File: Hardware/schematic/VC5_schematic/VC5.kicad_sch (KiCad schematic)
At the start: 2 parts, among them J1 Debug_output

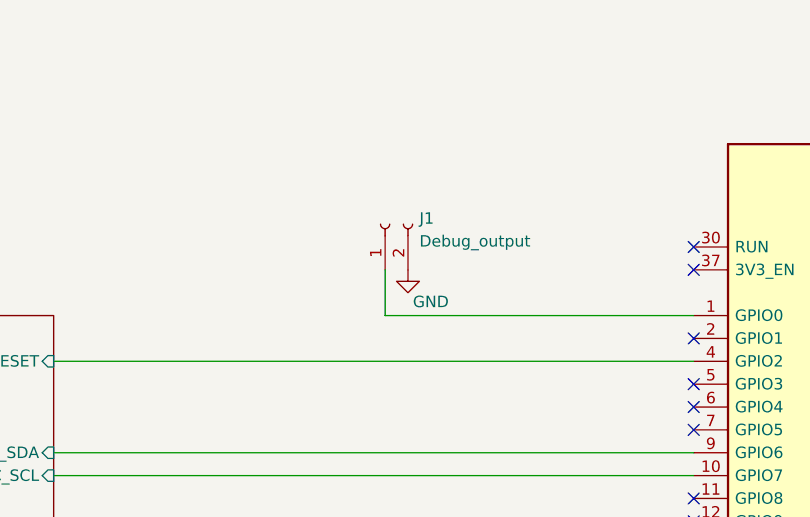
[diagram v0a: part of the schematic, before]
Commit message: fixed an error in the filters for the rotaries
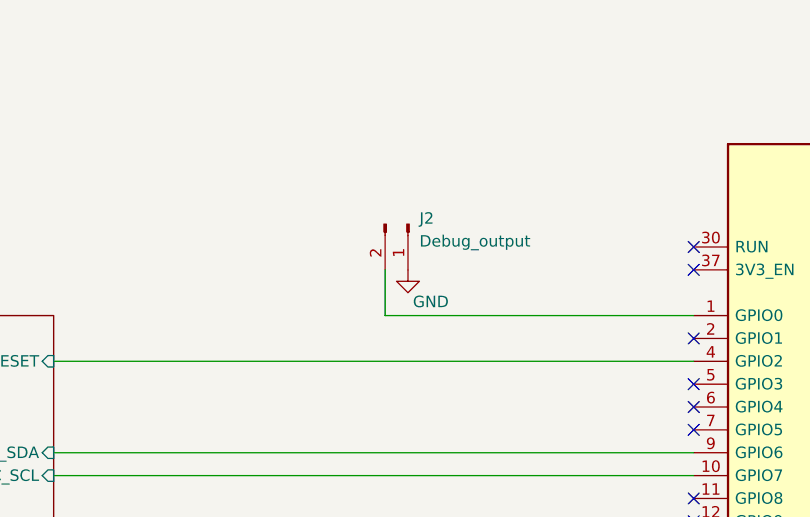
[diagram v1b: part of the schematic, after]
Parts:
- removed J1: Debug_output, symbol Connector:Conn_01x02_Socket
- added J2: Debug_output, Connector_PinHeader_2.54mm:PinHeader_1x02_P2.54mm_Vertical, symbol Connector:Conn_01x02_Pin
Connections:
- net GND: now also J2.1 (Pin_1)
- net at A1.1 (GPIO0): now also J2.2 (Pin_2)
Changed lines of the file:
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@@
-	)
-	(symbol
-		(lib_id "Connector:Conn_01x02_Socket")
-		(at 96.52 45.72 90)
-		(unit 1)
-		(exclude_from_sim no)
-		(in_bom yes)
-		(on_board yes)
-		(dnp no)
-		(fields_autoplaced yes)
-		(property "Reference" "J1"
-			(at 100.33 45.0849 90)
-			(effects
-				(font
-					(size 1.27 1.27)
-				)
-				(justify right)
-			)
-		)
-		(property "Value" "Debug_output"
-			(at 100.33 47.6249 90)
-			(effects
-				(font
-					(size 1.27 1.27)
-				)
-				(justify right)
-			)
-		)
-		(property "Footprint" ""
-			(at 96.52 45.72 0)
-			(effects
-				(font
-					(size 1.27 1.27)
-				)
-				(hide yes)
-			)
-		)
-		(property "Datasheet" "~"
-			(at 96.52 45.72 0)
-			(effects
-				(font
-					(size 1.27 1.27)
-				)
-				(hide yes)
-			)
-		)
-		(property "Description" "Generic connector, single row, 01x02, script generated"
-			(at 96.52 45.72 0)
-			(effects
-				(font
-					(size 1.27 1.27)
-				)
-				(hide yes)
-			)
-		)
-		(pin "1"
-		)
-		(pin "2"
-		)
-		(instances
-			(project ""
-				(path "/5ac87209-2525-401a-b136-a9d04031b521"
-					(reference "J1")
-					(unit 1)
-				)
-			)
-		)
 	)
 	(symbol
@@
 					(unit 1)
 				)
+			)
+		)
+	)
+	(symbol
+		(lib_id "Connector:Conn_01x02_Pin")
+		(at 99.06 45.72 270)
+		(unit 1)
+		(exclude_from_sim no)
+		(in_bom yes)
+		(on_board yes)
+		(dnp no)
+		(fields_autoplaced yes)
+		(property "Reference" "J2"
+			(at 100.33 45.0849 90)
+			(effects
+				(font
+					(size 1.27 1.27)
+				)
+				(justify left)
+			)
+		)
+		(property "Value" "Debug_output"
+			(at 100.33 47.6249 90)
+			(effects
+				(font
+					(size 1.27 1.27)
+				)
+				(justify left)
+			)
+		)
+		(property "Footprint" "Connector_PinHeader_2.54mm:PinHeader_1x02_P2.54mm_Vertical"
+			(at 99.06 45.72 0)
+			(effects
+				(font
+					(size 1.27 1.27)
+				)
+				(hide yes)
+			)
+		)
+		(property "Datasheet" "~"
+			(at 99.06 45.72 0)
+			(effects
+				(font
+					(size 1.27 1.27)
+				)
+				(hide yes)
+			)
+		)
+		(property "Description" "Generic connector, single row, 01x02, script generated"
+			(at 99.06 45.72 0)
+			(effects
+				(font
+					(size 1.27 1.27)
+				)
+				(hide yes)
+			)
+		)
+		(pin "1"
+		)
+		(pin "2"
+		)
+		(instances
+			(project ""
+				(path "/5ac87209-2525-401a-b136-a9d04031b521"
+					(reference "J2")
+					(unit 1)
+				)

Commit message: updated footprints and corresponding 3D models
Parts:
- A1: footprint Module:RaspberryPi_Pico_Common_THT -> VC5_footprint_library:RaspberryPi_Pico_Common_THT_custom
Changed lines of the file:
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@@
 			)
 		)
-		(property "Footprint" "Module:RaspberryPi_Pico_Common_THT"
+		(property "Footprint" "VC5_footprint_library:RaspberryPi_Pico_Common_THT_custom"
 			(at 153.67 118.11 0)
 			(effects

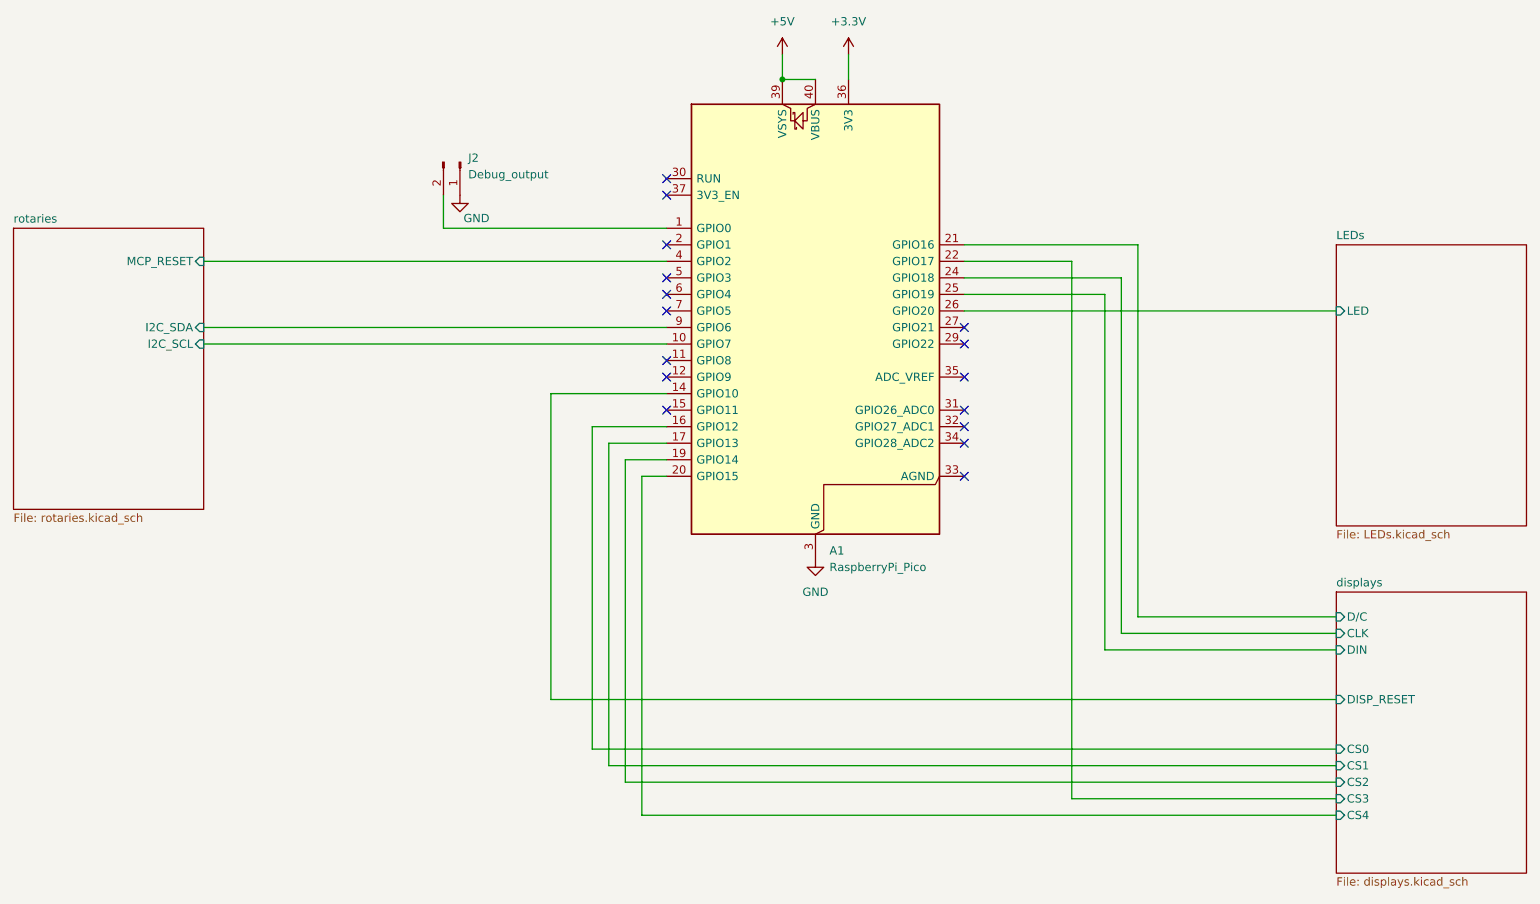
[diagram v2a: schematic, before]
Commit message: trace routing completed
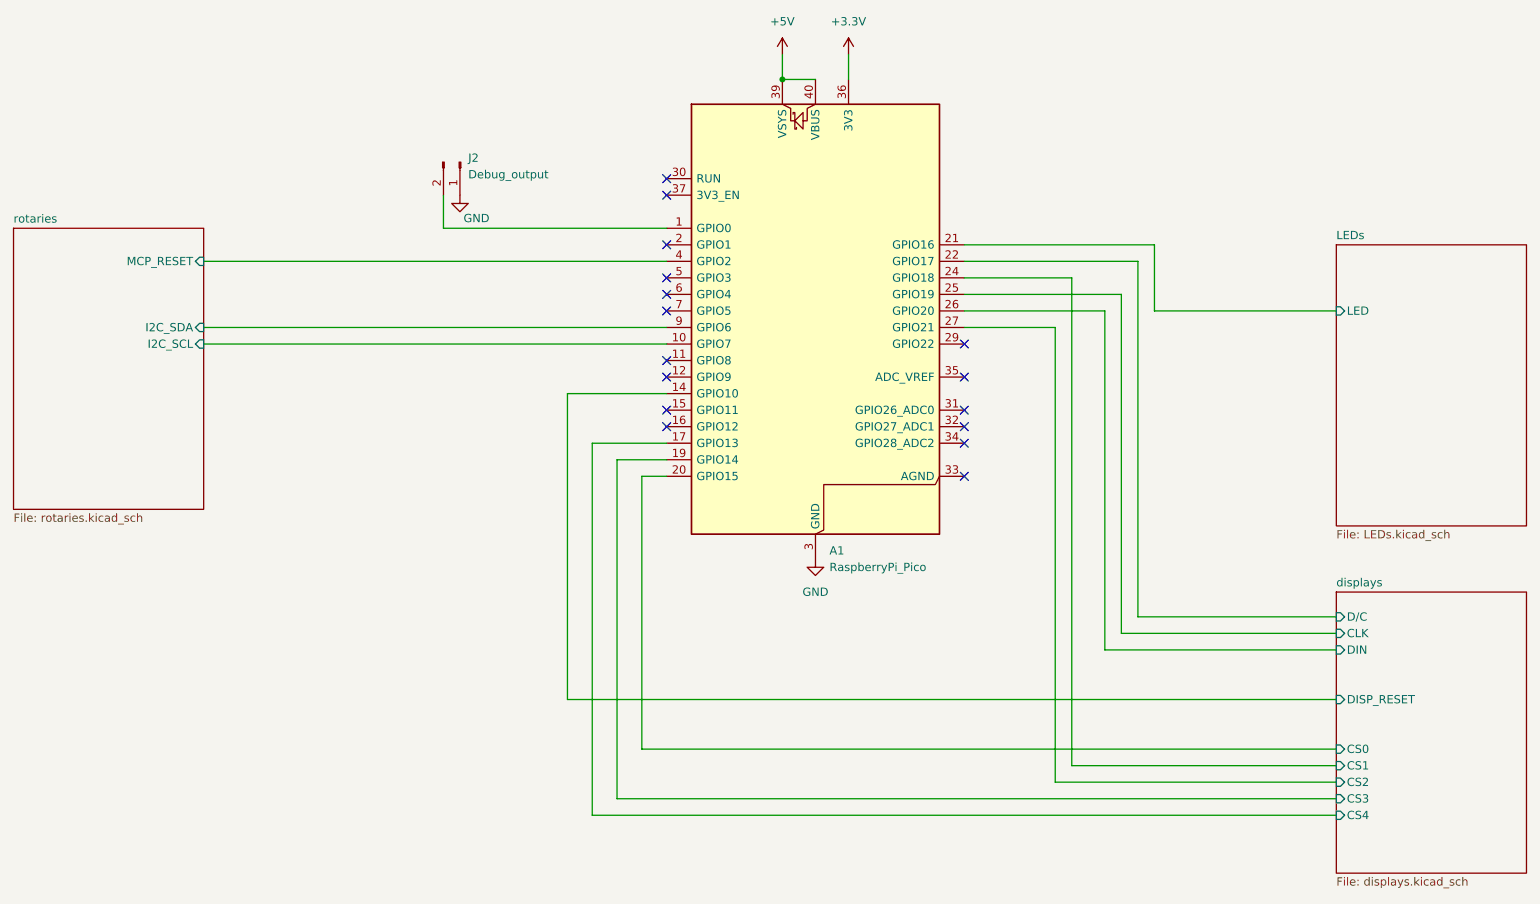
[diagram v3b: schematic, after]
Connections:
- net LEDs/LED: now also A1.21 (GPIO16); no longer A1.26 (GPIO20)
- net displays/CLK: now also A1.25 (GPIO19); no longer A1.24 (GPIO18)
- net displays/CS0: now also A1.20 (GPIO15); no longer A1.16 (GPIO12)
- net displays/CS1: now also A1.24 (GPIO18); no longer A1.17 (GPIO13)
- net displays/CS2: now also A1.27 (GPIO21); no longer A1.19 (GPIO14)
- net displays/CS3: now also A1.19 (GPIO14); no longer A1.22 (GPIO17)
- net displays/CS4: now also A1.17 (GPIO13); no longer A1.20 (GPIO15)
- net displays/DIN: now also A1.26 (GPIO20); no longer A1.25 (GPIO19)
- net displays/D/C: now also A1.22 (GPIO17); no longer A1.21 (GPIO16)
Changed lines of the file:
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@@
+	)
+	(no_connect
+		(at 130.81 86.36)
 	)
 	(no_connect
@@
 	)
 	(no_connect
-		(at 176.53 71.12)
-	)
-	(no_connect
 		(at 130.81 78.74)
 	)
@@
 	(wire
 		(pts
-			(xy 203.2 115.57) (xy 203.2 58.42)
-		)
-		(stroke
-			(width 0)
-			(type default)
-		)
-	)
-	(wire
-		(pts
-			(xy 124.46 91.44) (xy 130.81 91.44)
+			(xy 176.53 71.12) (xy 190.5 71.12)
+		)
+		(stroke
+			(width 0)
+			(type default)
+		)
+	)
+	(wire
+		(pts
+			(xy 203.2 115.57) (xy 203.2 60.96)
 		)
 		(stroke
@@
 	(wire
 		(pts
-			(xy 121.92 88.9) (xy 130.81 88.9)
+			(xy 190.5 140.97) (xy 233.68 140.97)
 		)
 		(stroke
@@
 	(wire
 		(pts
-			(xy 200.66 63.5) (xy 176.53 63.5)
-		)
-		(stroke
-			(width 0)
-			(type default)
-		)
-	)
-	(wire
-		(pts
-			(xy 113.03 128.27) (xy 113.03 81.28)
-		)
-		(stroke
-			(width 0)
-			(type default)
-		)
-	)
-	(wire
-		(pts
-			(xy 198.12 66.04) (xy 176.53 66.04)
-		)
-		(stroke
-			(width 0)
-			(type default)
-		)
-	)
-	(wire
-		(pts
-			(xy 121.92 138.43) (xy 121.92 88.9)
-		)
-		(stroke
-			(width 0)
-			(type default)
-		)
-	)
-	(wire
-		(pts
-			(xy 200.66 118.11) (xy 200.66 63.5)
+			(xy 193.04 138.43) (xy 233.68 138.43)
+		)
+		(stroke
+			(width 0)
+			(type default)
+		)
+	)
+	(wire
+		(pts
+			(xy 115.57 128.27) (xy 115.57 81.28)
+		)
+		(stroke
+			(width 0)
+			(type default)
+		)
+	)
+	(wire
+		(pts
+			(xy 119.38 146.05) (xy 233.68 146.05)
+		)
+		(stroke
+			(width 0)
+			(type default)
+		)
+	)
+	(wire
+		(pts
+			(xy 119.38 88.9) (xy 130.81 88.9)
+		)
+		(stroke
+			(width 0)
+			(type default)
+		)
+	)
+	(wire
+		(pts
+			(xy 127 93.98) (xy 127 135.89)
+		)
+		(stroke
+			(width 0)
+			(type default)
+		)
+	)
+	(wire
+		(pts
+			(xy 200.66 118.11) (xy 200.66 66.04)
 		)
 		(stroke
@@
 	(wire
 		(pts
-			(xy 198.12 120.65) (xy 198.12 66.04)
-		)
-		(stroke
-			(width 0)
-			(type default)
-		)
-	)
-	(wire
-		(pts
-			(xy 193.04 143.51) (xy 233.68 143.51)
-		)
-		(stroke
-			(width 0)
-			(type default)
-		)
-	)
-	(wire
-		(pts
-			(xy 119.38 86.36) (xy 130.81 86.36)
+			(xy 193.04 63.5) (xy 193.04 138.43)
+		)
+		(stroke
+			(width 0)
+			(type default)
+		)
+	)
+	(wire
+		(pts
+			(xy 198.12 120.65) (xy 198.12 68.58)
+		)
+		(stroke
+			(width 0)
+			(type default)
+		)
+	)
+	(wire
+		(pts
+			(xy 127 135.89) (xy 233.68 135.89)
+		)
+		(stroke
+			(width 0)
+			(type default)
+		)
+	)
+	(wire
+		(pts
+			(xy 123.19 91.44) (xy 130.81 91.44)
+		)
+		(stroke
+			(width 0)
+			(type default)
+		)
+	)
+	(wire
+		(pts
+			(xy 176.53 66.04) (xy 200.66 66.04)
 		)
 		(stroke
@@
 	(wire
 		(pts
-			(xy 124.46 140.97) (xy 124.46 91.44)
-		)
-		(stroke
-			(width 0)
-			(type default)
-		)
-	)
-	(wire
-		(pts
-			(xy 113.03 81.28) (xy 130.81 81.28)
-		)
-		(stroke
-			(width 0)
-			(type default)
-		)
-	)
-	(wire
-		(pts
-			(xy 124.46 140.97) (xy 233.68 140.97)
-		)
-		(stroke
-			(width 0)
-			(type default)
-		)
-	)
-	(wire
-		(pts
-			(xy 113.03 128.27) (xy 233.68 128.27)
-		)
-		(stroke
-			(width 0)
-			(type default)
-		)
-	)
-	(wire
-		(pts
-			(xy 127 146.05) (xy 233.68 146.05)
-		)
-		(stroke
-			(width 0)
-			(type default)
-		)
-	)
-	(wire
-		(pts
-			(xy 121.92 138.43) (xy 233.68 138.43)
+			(xy 115.57 81.28) (xy 130.81 81.28)
+		)
+		(stroke
+			(width 0)
+			(type default)
+		)
+	)
+	(wire
+		(pts
+			(xy 123.19 143.51) (xy 123.19 91.44)
+		)
+		(stroke
+			(width 0)
+			(type default)
+		)
+	)
+	(wire
+		(pts
+			(xy 123.19 143.51) (xy 233.68 143.51)
+		)
+		(stroke
+			(width 0)
+			(type default)
+		)
+	)
+	(wire
+		(pts
+			(xy 205.74 58.42) (xy 176.53 58.42)
+		)
+		(stroke
+			(width 0)
+			(type default)
+		)
+	)
+	(wire
+		(pts
+			(xy 119.38 146.05) (xy 119.38 88.9)
+		)
+		(stroke
+			(width 0)
+			(type default)
+		)
+	)
+	(wire
+		(pts
+			(xy 130.81 93.98) (xy 127 93.98)
+		)
+		(stroke
+			(width 0)
+			(type default)
+		)
+	)
+	(wire
+		(pts
+			(xy 115.57 128.27) (xy 233.68 128.27)
+		)
+		(stroke
+			(width 0)
+			(type default)
+		)
+	)
+	(wire
+		(pts
+			(xy 176.53 63.5) (xy 193.04 63.5)
 		)
 		(stroke
@@
 	(wire
 		(pts
-			(xy 119.38 135.89) (xy 119.38 86.36)
-		)
-		(stroke
-			(width 0)
-			(type default)
-		)
-	)
-	(wire
-		(pts
-			(xy 127 93.98) (xy 130.81 93.98)
-		)
-		(stroke
-			(width 0)
-			(type default)
-		)
-	)
-	(wire
-		(pts
-			(xy 193.04 143.51) (xy 193.04 60.96)
+			(xy 233.68 68.58) (xy 205.74 68.58)
 		)
 		(stroke
@@
 	(wire
 		(pts
-			(xy 119.38 135.89) (xy 233.68 135.89)
-		)
-		(stroke
-			(width 0)
-			(type default)
-		)
-	)
-	(wire
-		(pts
-			(xy 127 146.05) (xy 127 93.98)
-		)
-		(stroke
-			(width 0)
-			(type default)
-		)
-	)
-	(wire
-		(pts
-			(xy 176.53 68.58) (xy 233.68 68.58)
+			(xy 176.53 68.58) (xy 198.12 68.58)
+		)
+		(stroke
+			(width 0)
+			(type default)
+		)
+	)
+	(wire
+		(pts
+			(xy 205.74 68.58) (xy 205.74 58.42)
+		)
+		(stroke
+			(width 0)
+			(type default)
+		)
+	)
+	(wire
+		(pts
+			(xy 190.5 71.12) (xy 190.5 140.97)
 		)
 		(stroke
@@
 	(wire
 		(pts
-			(xy 193.04 60.96) (xy 176.53 60.96)
-		)
-		(stroke
-			(width 0)
-			(type default)
-		)
-	)
-	(wire
-		(pts
-			(xy 203.2 58.42) (xy 176.53 58.42)
-		)
-		(stroke
+			(xy 176.53 60.96) (xy 203.2 60.96)
+		)
+		(stroke

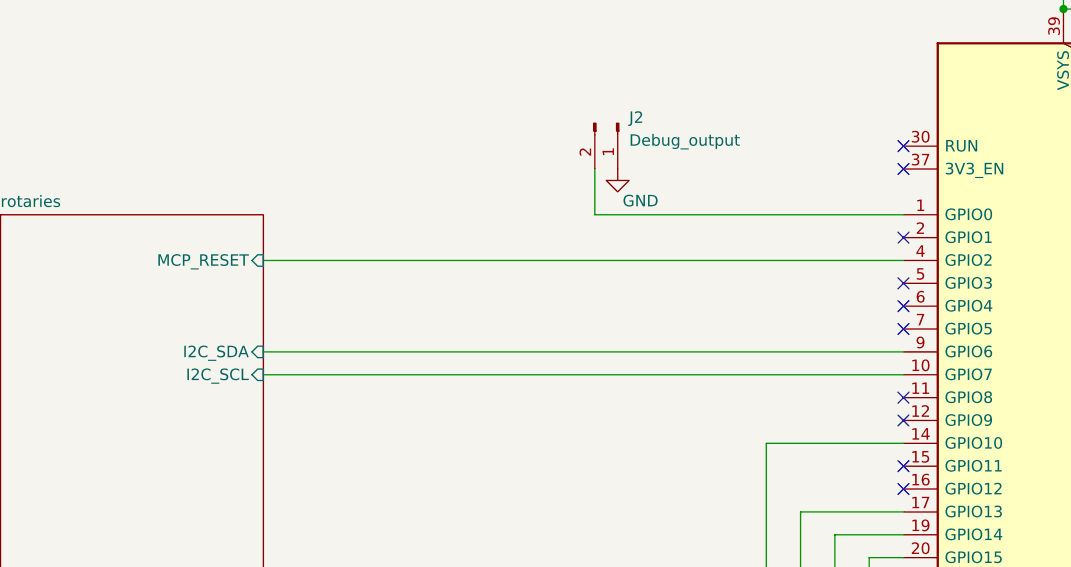
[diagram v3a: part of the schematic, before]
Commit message: fixed missing interrupt line
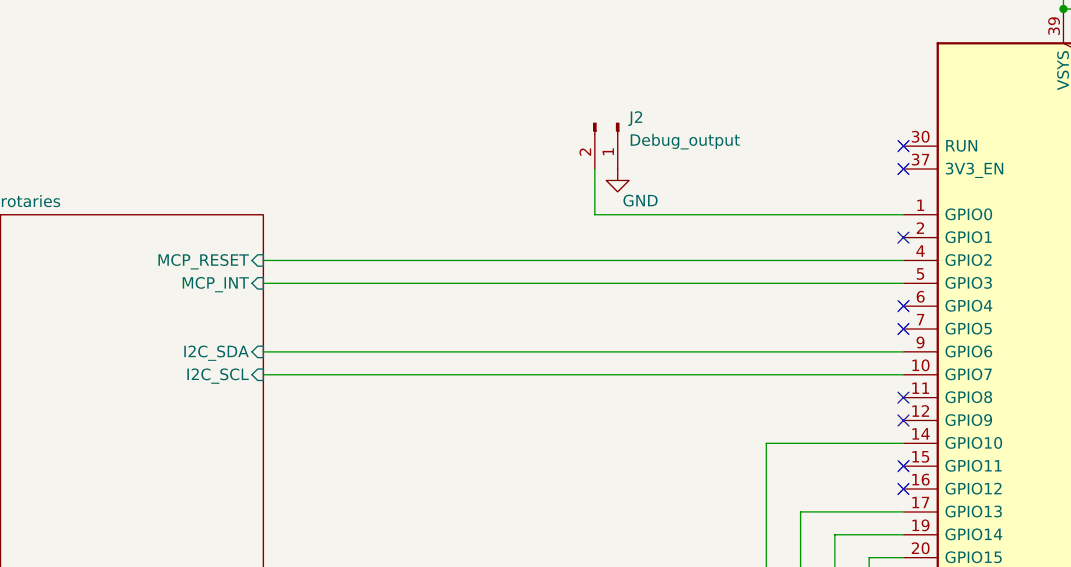
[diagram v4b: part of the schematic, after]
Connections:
- net rotaries/MCP_INT: now reaches A1.5 (GPIO3)
- no-connect marks 16 -> 15
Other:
- sheet rotaries ports: added MCP_INT; removed none
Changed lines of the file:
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@@
-	)
-	(no_connect
-		(at 130.81 63.5)
 	)
 	(no_connect
@@
 		(pts
 			(xy 59.69 71.12) (xy 130.81 71.12)
+		)
+		(stroke
+			(width 0)
+			(type default)
+		)
+	)
+	(wire
+		(pts
+			(xy 59.69 63.5) (xy 130.81 63.5)
 		)
 		(stroke
@@
 			(effects
 				(font
+					(size 1.27 1.27)
+				)
+				(justify right)
+			)
+		)
+		(pin "MCP_INT" input
+			(at 59.69 63.5 0)
+			(effects
+				(font
